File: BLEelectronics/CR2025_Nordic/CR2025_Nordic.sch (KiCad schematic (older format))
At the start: 31 parts, among them IC1 LTC4412xS6, IC2 PCF8523T, IC3 MX25R6435FM2IL0, IC4 LTC4054LES5-4.2#TRPBF, J1 Nordic_nRF52840_breakout, J4 Conn_01x01_Female, Q1 Si2307CDS, U1 LP5907MFX-3.3, U2 BAT-HLD-001, U3 ESD401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

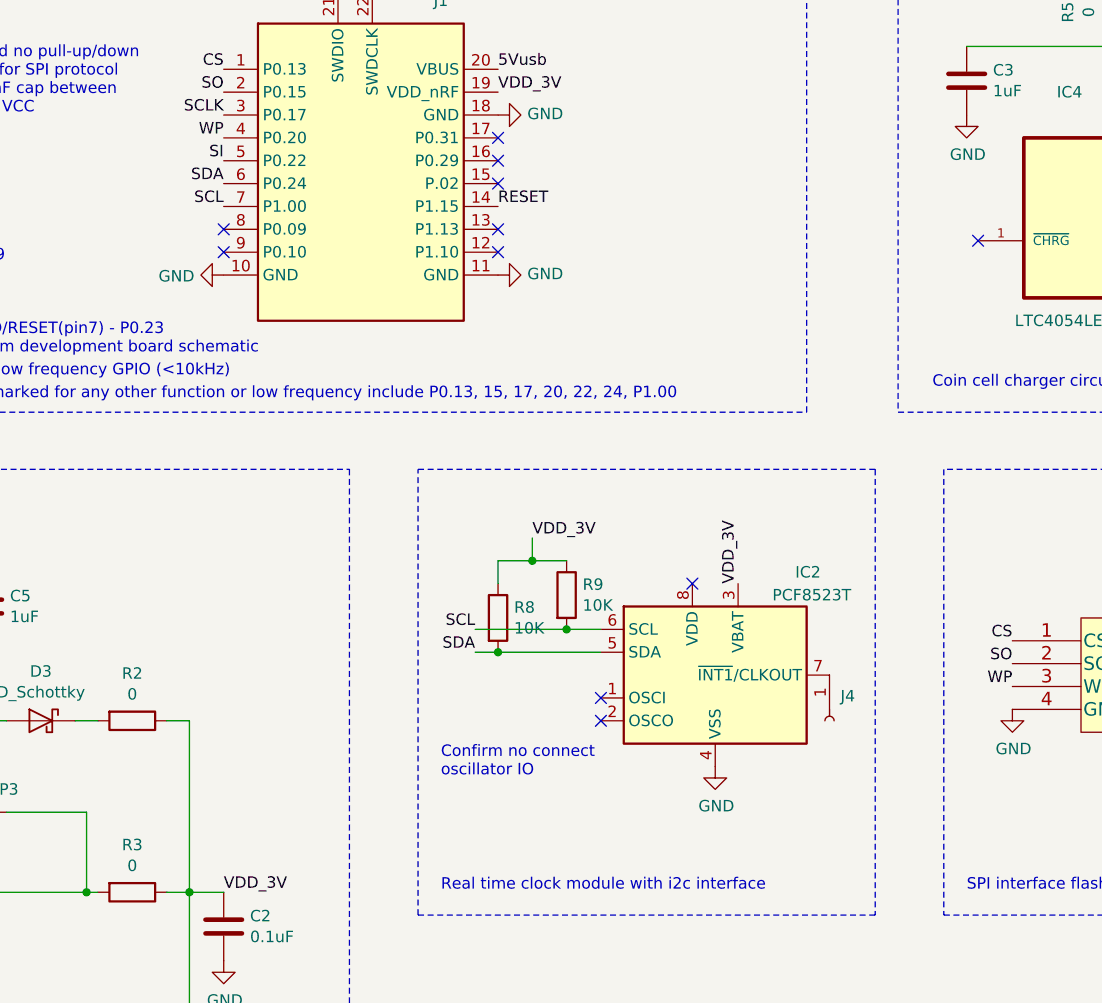
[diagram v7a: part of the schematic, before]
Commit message: Moved power from pin 3 VBat to pin 8 Vdd on RTC. Swapped SIO3 and SDA on 1a and 1b. Changed battery footprint to allow backside routing for Flash and USB data. Todo: Unbreak MVP1B layout rerouting.
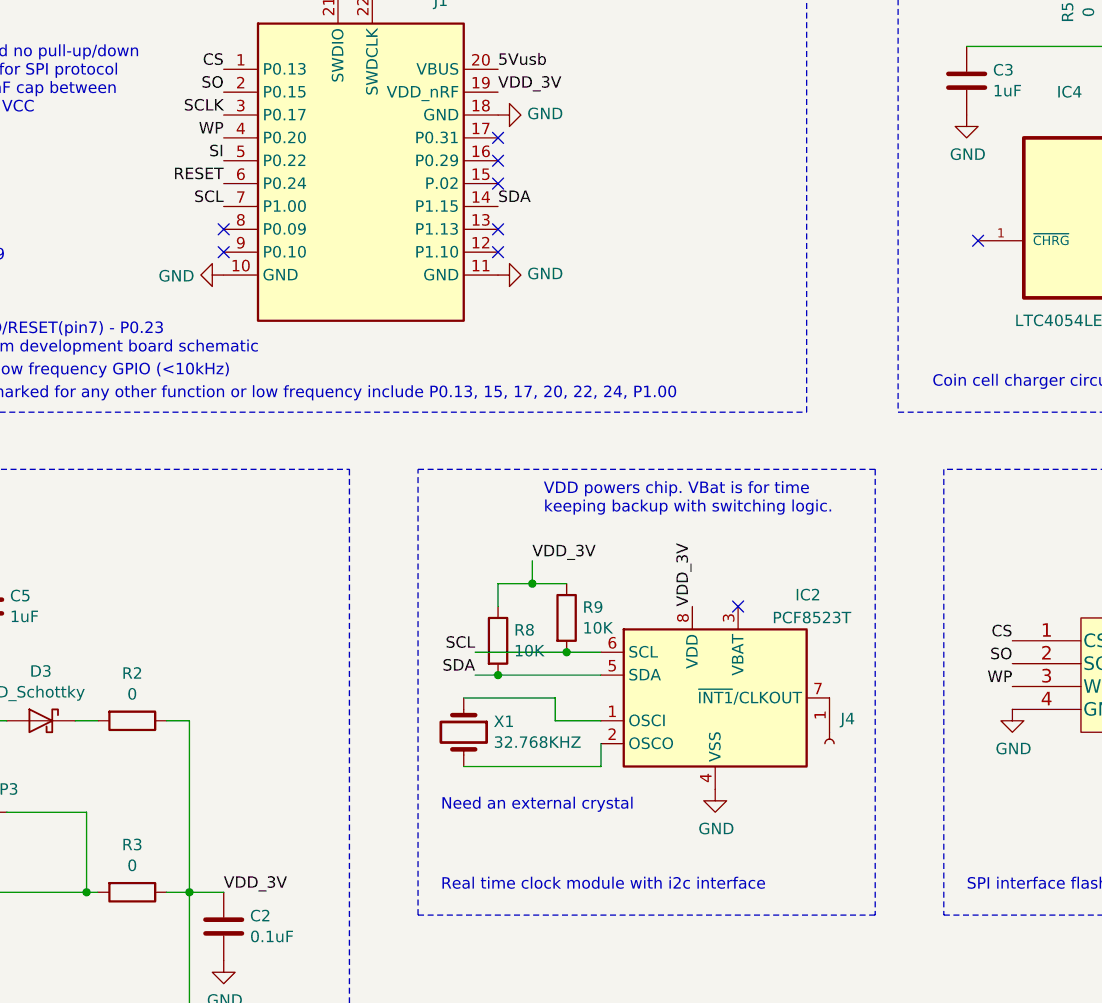
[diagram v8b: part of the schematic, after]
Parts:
- added X1: 32.768KHZ, Crystal:Crystal_SMD_3215-2Pin_3.2x1.5mm, symbol Device:Crystal
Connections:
- wire segments 64 -> 69
- no-connect marks 13 -> 11
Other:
- note added: "Need an external crystal"
- note added: "VDD powers chip. VBat is for time \nkeeping backup with switching logic."
- note removed: "Confirm no connect\noscillator IO"
- moved on the sheet: IC2, J4, R8, R9
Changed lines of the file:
@@
 L Timer_RTC:PCF8523T IC2
 U 1 1 5E9F84DB
-P 7450 4150
-F 0 "IC2" H 7800 4600 50  0000 L CNN
-F 1 "PCF8523T" H 7700 4500 50  0000 L CNN
-F 2 "Package_SO:SOIC-8_3.9x4.9mm_P1.27mm" H 8250 3800 50  0001 C CNN
-F 3 "https://www.nxp.com/docs/en/data-sheet/PCF8523.pdf" H 7450 4150 50  0001 C CNN
-F 4 "NXP USA Inc." H 300 50  50  0001 C CNN "MFR"
-F 5 "PCF8523T/1,118" H 300 50  50  0001 C CNN "MPN"
-F 6 "568-5306-1-ND" H 300 50  50  0001 C CNN "DPN"
-F 7 "-" H 300 50  50  0001 C CNN "LCSCPN"
-F 8 "-" H 300 50  50  0001 C CNN "SPR"
-F 9 "-" H 300 50  50  0001 C CNN "SPN"
-F 10 "-" H 300 50  50  0001 C CNN "SIM"
-	1    7450 4150
+P 7450 4250
+F 0 "IC2" H 7800 4700 50  0000 L CNN
+F 1 "PCF8523T" H 7700 4600 50  0000 L CNN
+F 2 "Package_SO:SOIC-8_3.9x4.9mm_P1.27mm" H 8250 3900 50  0001 C CNN
+F 3 "https://www.nxp.com/docs/en/data-sheet/PCF8523.pdf" H 7450 4250 50  0001 C CNN
+F 4 "NXP USA Inc." H 300 150 50  0001 C CNN "MFR"
+F 5 "PCF8523T/1,118" H 300 150 50  0001 C CNN "MPN"
+F 6 "568-5306-1-ND" H 300 150 50  0001 C CNN "DPN"
+F 7 "-" H 300 150 50  0001 C CNN "LCSCPN"
+F 8 "-" H 300 150 50  0001 C CNN "SPR"
+F 9 "-" H 300 150 50  0001 C CNN "SPN"
+F 10 "-" H 300 150 50  0001 C CNN "SIM"
+	1    7450 4250
 	1    0    0    -1
 $EndComp
@@
 L power:GND #PWR0101
 U 1 1 5EA0EA9A
-P 7450 4550
-F 0 "#PWR0101" H 7450 4300 50  0001 C CNN
-F 1 "GND" H 7455 4377 50  0000 C CNN
-F 2 "" H 7450 4550 50  0001 C CNN
-F 3 "" H 7450 4550 50  0001 C CNN
-	1    7450 4550
+P 7450 4650
+F 0 "#PWR0101" H 7450 4400 50  0001 C CNN
+F 1 "GND" H 7455 4477 50  0000 C CNN
+F 2 "" H 7450 4650 50  0001 C CNN
+F 3 "" H 7450 4650 50  0001 C CNN
+	1    7450 4650
 	1    0    0    -1
 $EndComp
@@
 L Device:R R9
 U 1 1 5EA074F4
-P 6800 3800
-F 0 "R9" H 6870 3846 50  0000 L CNN
-F 1 "10K" H 6870 3755 50  0000 L CNN
-F 2 "Resistor_SMD:R_0603_1608Metric_Pad1.05x0.95mm_HandSolder" V 6730 3800 50  0001 C CNN
-F 3 "https://www.yageo.com/upload/media/product/productsearch/datasheet/rchip/PYu-RC_Group_51_RoHS_L_10.pdf" H 6800 3800 50  0001 C CNN
-F 4 "Yageo" H 350 50  50  0001 C CNN "MFR"
-F 5 "RC0603JR-0710KL" H 350 50  50  0001 C CNN "MPN"
-F 6 "311-10KGRCT-ND" H 350 50  50  0001 C CNN "DPN"
-F 7 "-" H 350 50  50  0001 C CNN "LCSCPN"
-F 8 "-" H 350 50  50  0001 C CNN "SPR"
-F 9 "-" H 350 50  50  0001 C CNN "SPN"
-F 10 "-" H 350 50  50  0001 C CNN "SIM"
-	1    6800 3800
+P 6800 3900
+F 0 "R9" H 6870 3946 50  0000 L CNN
+F 1 "10K" H 6870 3855 50  0000 L CNN
+F 2 "Resistor_SMD:R_0603_1608Metric_Pad1.05x0.95mm_HandSolder" V 6730 3900 50  0001 C CNN
+F 3 "https://www.yageo.com/upload/media/product/productsearch/datasheet/rchip/PYu-RC_Group_51_RoHS_L_10.pdf" H 6800 3900 50  0001 C CNN
+F 4 "Yageo" H 350 150 50  0001 C CNN "MFR"
+F 5 "RC0603JR-0710KL" H 350 150 50  0001 C CNN "MPN"
+F 6 "311-10KGRCT-ND" H 350 150 50  0001 C CNN "DPN"
+F 7 "-" H 350 150 50  0001 C CNN "LCSCPN"
+F 8 "-" H 350 150 50  0001 C CNN "SPR"
+F 9 "-" H 350 150 50  0001 C CNN "SPN"
+F 10 "-" H 350 150 50  0001 C CNN "SIM"
+	1    6800 3900
 	1    0    0    -1
 $EndComp
@@
 L Device:R R8
 U 1 1 5EA0D031
-P 6500 3900
-F 0 "R8" H 6570 3946 50  0000 L CNN
-F 1 "10K" H 6570 3855 50  0000 L CNN
-F 2 "Resistor_SMD:R_0603_1608Metric_Pad1.05x0.95mm_HandSolder" V 6430 3900 50  0001 C CNN
-F 3 "https://www.yageo.com/upload/media/product/productsearch/datasheet/rchip/PYu-RC_Group_51_RoHS_L_10.pdf" H 6500 3900 50  0001 C CNN
-F 4 "Yageo" H 50  150 50  0001 C CNN "MFR"
-F 5 "RC0603JR-0710KL" H 50  150 50  0001 C CNN "MPN"
-F 6 "311-10KGRCT-ND" H 50  150 50  0001 C CNN "DPN"
-F 7 "-" H 50  150 50  0001 C CNN "LCSCPN"
-F 8 "-" H 50  150 50  0001 C CNN "SPR"
-F 9 "-" H 50  150 50  0001 C CNN "SPN"
-F 10 "-" H 50  150 50  0001 C CNN "SIM"
-	1    6500 3900
+P 6500 4000
+F 0 "R8" H 6570 4046 50  0000 L CNN
+F 1 "10K" H 6570 3955 50  0000 L CNN
+F 2 "Resistor_SMD:R_0603_1608Metric_Pad1.05x0.95mm_HandSolder" V 6430 4000 50  0001 C CNN
+F 3 "https://www.yageo.com/upload/media/product/productsearch/datasheet/rchip/PYu-RC_Group_51_RoHS_L_10.pdf" H 6500 4000 50  0001 C CNN
+F 4 "Yageo" H 50  250 50  0001 C CNN "MFR"
+F 5 "RC0603JR-0710KL" H 50  250 50  0001 C CNN "MPN"
+F 6 "311-10KGRCT-ND" H 50  250 50  0001 C CNN "DPN"
+F 7 "-" H 50  250 50  0001 C CNN "LCSCPN"
+F 8 "-" H 50  250 50  0001 C CNN "SPR"
+F 9 "-" H 50  250 50  0001 C CNN "SPN"
+F 10 "-" H 50  250 50  0001 C CNN "SIM"
+	1    6500 4000
 	1    0    0    -1
 $EndComp
@@
 L Connector:Conn_01x01_Female J4
 U 1 1 5EA8C546
-P 7950 4350
-F 0 "J4" V 7842 4398 50  0000 L CNN
-F 1 "Conn_01x01_Female" H 7978 4285 50  0001 L CNN
-F 2 "Connector_PinHeader_2.54mm:PinHeader_1x01_P2.54mm_Vertical" H 7950 4350 50  0001 C CNN
-F 3 "~" H 7950 4350 50  0001 C CNN
-F 4 "-" H 0   0   50  0001 C CNN "MFR"
-F 5 "-" H 0   0   50  0001 C CNN "MPN"
-F 6 "-" H 0   0   50  0001 C CNN "DPN"
-F 7 "-" H 0   0   50  0001 C CNN "LCSCPN"
-F 8 "-" H 0   0   50  0001 C CNN "SPR"
-F 9 "-" H 0   0   50  0001 C CNN "SPN"
-F 10 "-" H 0   0   50  0001 C CNN "SIM"
-	1    7950 4350
+P 7950 4450
+F 0 "J4" V 7842 4498 50  0000 L CNN
+F 1 "Conn_01x01_Female" H 7978 4385 50  0001 L CNN
+F 2 "Connector_PinHeader_2.54mm:PinHeader_1x01_P2.54mm_Vertical" H 7950 4450 50  0001 C CNN
+F 3 "~" H 7950 4450 50  0001 C CNN
+F 4 "-" H 0   100 50  0001 C CNN "MFR"
+F 5 "-" H 0   100 50  0001 C CNN "MPN"
+F 6 "-" H 0   100 50  0001 C CNN "DPN"
+F 7 "-" H 0   100 50  0001 C CNN "LCSCPN"
+F 8 "-" H 0   100 50  0001 C CNN "SPR"
+F 9 "-" H 0   100 50  0001 C CNN "SPN"
+F 10 "-" H 0   100 50  0001 C CNN "SIM"
+	1    7950 4450
 	0    1    1    0
 $EndComp
@@
 Text Label 10400 4000 0    50   ~ 0
 VDD_3V
-Text Label 7550 3750 1    50   ~ 0
+Text Label 7350 3850 1    50   ~ 0
 VDD_3V
 Text Notes 6250 5100 0    50   ~ 0
@@
 Text Notes 3950 2950 0    50   ~ 0
 GPIO not marked for any other function or low frequency include P0.13, 15, 17, 20, 22, 24, P1.00
-Text Label 6400 3950 2    50   ~ 0
+Text Label 6400 4050 2    50   ~ 0
 SCL
-Text Label 6400 4050 2    50   ~ 0
+Text Label 6400 4150 2    50   ~ 0
 SDA
 Text Label 8750 4100 2    50   ~ 0
@@
 Text Label 5300 1700 2    50   ~ 0
 SCLK
-Text Label 5300 2100 2    50   ~ 0
-SCL
-Text Label 5300 2000 2    50   ~ 0
-SDA
 Text Notes 3950 2850 0    50   ~ 0
 P1.15 is a low frequency GPIO (<10kHz)
@@
 Text Notes 4000 1700 0    50   ~ 0
 Confirmed no pull-up/down\nresistors for SPI protocol\nAdd 100nF cap between \nGND and VCC
-Text Label 6650 3550 0    50   ~ 0
+Text Label 6650 3650 0    50   ~ 0
 VDD_3V
 Text Notes 2600 1950 0    50   ~ 0
 TVS diode for ESD
-Text Notes 6250 4600 0    50   ~ 0
-Confirm no connect\noscillator IO
+Text Notes 6250 4750 0    50   ~ 0
+Need an external crystal
 Text Label 10400 4200 0    50   ~ 0
 SCLK
@@
 Text Notes 2550 3900 0    50   ~ 0
 TVS diode \nfor ESD\nprotection
-Text Label 6500 2100 0    50   ~ 0
+Text Label 5300 2000 2    50   ~ 0
 RESET
 Wire Wire Line
@@
 	10800 3250 8450 3250
 Wire Wire Line
-	6950 3950 6800 3950
-Wire Wire Line
-	6800 3950 6400 3950
-Wire Wire Line
-	6500 4050 6400 4050
-Wire Wire Line
-	6500 4050 6950 4050
-Wire Wire Line
-	6500 3750 6500 3650
-Wire Wire Line
-	6500 3650 6650 3650
-Wire Wire Line
-	6650 3650 6650 3550
-Wire Wire Line
-	6650 3650 6800 3650
+	6950 4050 6800 4050
+Wire Wire Line
+	6800 4050 6400 4050
+Wire Wire Line
+	6500 4150 6400 4150
+Wire Wire Line
+	6500 4150 6950 4150
+Wire Wire Line
+	6500 3850 6500 3750
+Wire Wire Line
+	6500 3750 6650 3750
+Wire Wire Line
+	6650 3750 6650 3650
+Wire Wire Line
+	6650 3750 6800 3750
 Wire Notes Line
 	1050 3250 5850 3250
@@
 Connection ~ 9900 2450
 Connection ~ 9200 1400
-Connection ~ 6800 3950
-Connection ~ 6500 4050
-Connection ~ 6650 3650
+Connection ~ 6800 4050
+Connection ~ 6500 4150
+Connection ~ 6650 3750
 Connection ~ 5150 5100
 Connection ~ 3550 4350
@@
 NoConn ~ 6500 1900
 NoConn ~ 6500 1800
-NoConn ~ 6950 4350
-NoConn ~ 6950 4250
-NoConn ~ 7350 3750
 NoConn ~ 5800 1150
 NoConn ~ 5950 1150
@@
 Wire Wire Line
 	1600 5100 3400 5100
+NoConn ~ 7550 3850
+Text Notes 6700 3450 0    50   ~ 0
+VDD powers chip. VBat is for time \nkeeping backup with switching logic.
+$Comp
+L Device:Crystal X1
+U 1 1 5EB305AF
+P 6350 4400
+F 0 "X1" V 6304 4531 50  0000 L CNN
+F 1 "32.768KHZ" V 6395 4531 50  0000 L CNN
+F 2 "Crystal:Crystal_SMD_3215-2Pin_3.2x1.5mm" H 6350 4400 50  0001 C CNN
+F 3 "https://www.microcrystal.com/fileadmin/Media/Products/32kHz/Datasheet/CM7V-T1A_Low-ESR.pdf" H 6350 4400 50  0001 C CNN
+F 4 "Micro Crystal AG" V 6350 4400 50  0001 C CNN "MFR"
+F 5 "CM7VT1A-LOWESR-32.768KHZ-12.5PF-20-TA-QC" V 6350 4400 50  0001 C CNN "MPN"
+F 6 "2195-CM7VT1ALOWESR32.768KHZ12.5PF20TAQCCT-ND" V 6350 4400 50  0001 C CNN "DPN"
+	1    6350 4400
+	0    1    1    0
+$EndComp
+Wire Wire Line
+	6950 4450 6950 4550
+Wire Wire Line
+	6950 4550 6350 4550
+Wire Wire Line
+	6950 4350 6750 4350
+Wire Wire Line
+	6750 4350 6750 4250
+Wire Wire Line
+	6750 4250 6350 4250
+Text Label 5300 2100 2    50   ~ 0
+SCL
+Text Label 6500 2100 0    50   ~ 0
+SDA
 $EndSCHEMATC
